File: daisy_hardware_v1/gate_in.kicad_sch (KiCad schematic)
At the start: 5 parts, among them J11 PJ398SM-12, Q6 MMBT3904

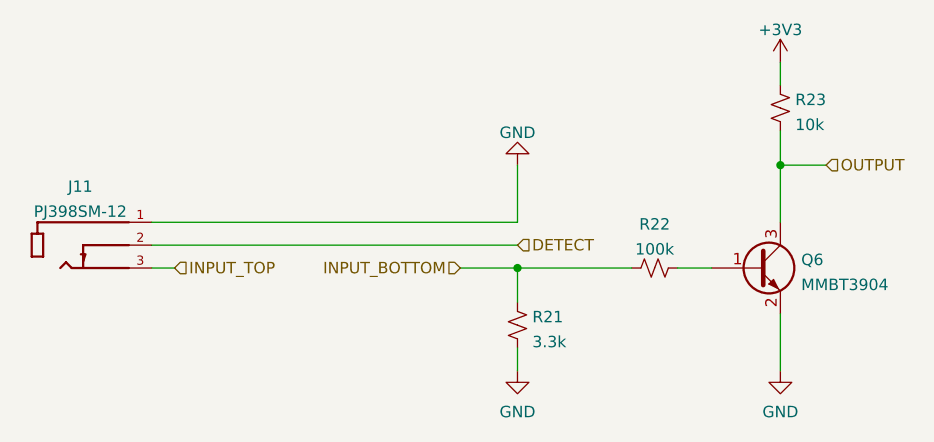
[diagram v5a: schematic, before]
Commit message: board connectors expanded
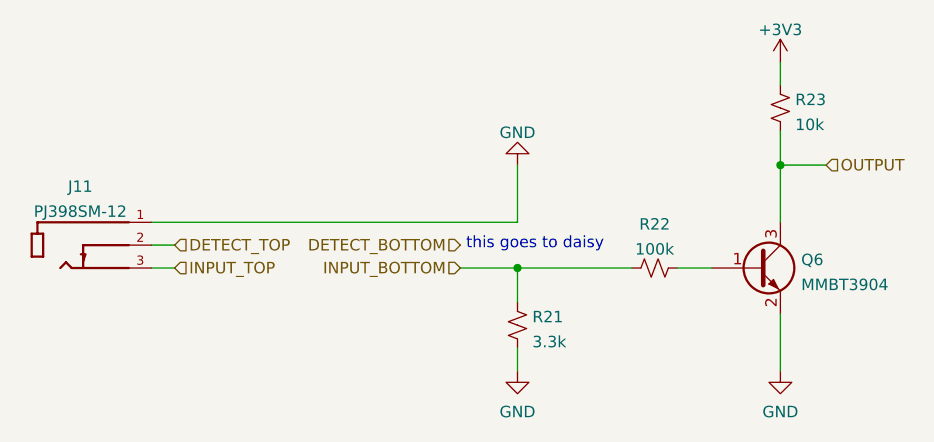
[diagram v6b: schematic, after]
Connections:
- net DETECT renamed DETECT_TOP
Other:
- note added: "this goes to daisy"
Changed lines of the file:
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@@
+    (stroke (width 0) (type default) (color 0 0 0 0))
+  )
+  (wire (pts (xy 52.07 106.68) (xy 54.61 106.68))
     (stroke (width 0) (type default) (color 0 0 0 0))
   )
@@
     (stroke (width 0) (type default) (color 0 0 0 0))
   )
-  (wire (pts (xy 52.07 106.68) (xy 92.71 106.68))
+  (wire (pts (xy 121.92 114.3) (xy 121.92 120.65))
     (stroke (width 0) (type default) (color 0 0 0 0))
   )
-  (wire (pts (xy 121.92 114.3) (xy 121.92 120.65))
-    (stroke (width 0) (type default) (color 0 0 0 0))
+  (text "this goes to daisy" (at 86.995 107.315 0)
+    (effects (font (size 1.27 1.27)) (justify left bottom))
   )
   (hierarchical_label "INPUT_BOTTOM" (shape input) (at 86.36 109.22 180)
@@
     (effects (font (size 1.27 1.27)) (justify left))
   )
-  (hierarchical_label "DETECT" (shape input) (at 92.71 106.68 0)
+  (hierarchical_label "DETECT_TOP" (shape input) (at 54.61 106.68 0)
     (effects (font (size 1.27 1.27)) (justify left))
   )
+  (hierarchical_label "DETECT_BOTTOM" (shape input) (at 86.36 106.68 180)
+    (effects (font (size 1.27 1.27)) (justify right))
+  )
   (hierarchical_label "OUTPUT" (shape input) (at 127 97.79 0)
